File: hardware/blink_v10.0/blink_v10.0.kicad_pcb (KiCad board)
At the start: 2 copper layers, 119 x 92 mm, 129 parts, among them J1 Conn_01x02, J11 KH-BNC50-3511, J12 KH-BNC50-3511, J13 KH-BNC50-3511, J14 Conn_02x16_Odd_Even, J15 Conn_01x01, J16 Conn_01x01, J2 PJ-320D, J3 PJ-320D, J4 KH-BNC50-3511, J5 Conn_01x06_Pin, J6 Conn_01x03, J7 Conn_01x06_Pin, J9 USB_C_Receptacle, Q3 2N7002, Q4 2N7002, Q5 2N7002, SW1 SW_SPDT, SW2 SW_Push_4PDT, SW3 SW_Push_4PDT, SW4 SW_Push_4PDT, U1 AMS1117-3.3, U10 TMP112AIDRLR, U2 AD8397, U3 M24C02-RMN, U4 STM32F405RGTx, U5 SN74LVC1G14DBV, U6 SN74LVC1G14DBV, U7 CH340C, U8 USBLC6-2P6, U9 MCP73832-2-OT, X1 GTXO-14V (2.048MHz), Y1 16MHz

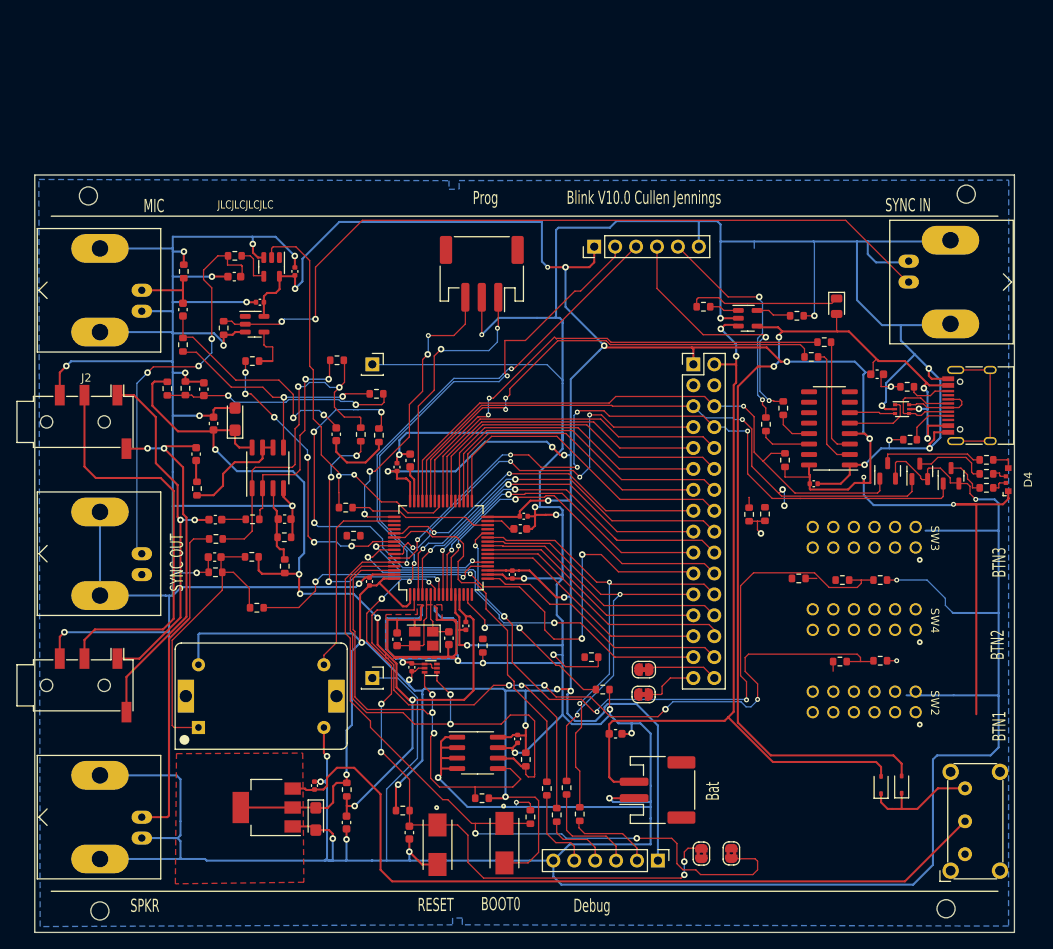
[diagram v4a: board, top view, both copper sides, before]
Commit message: add a sense resistor to blink v10
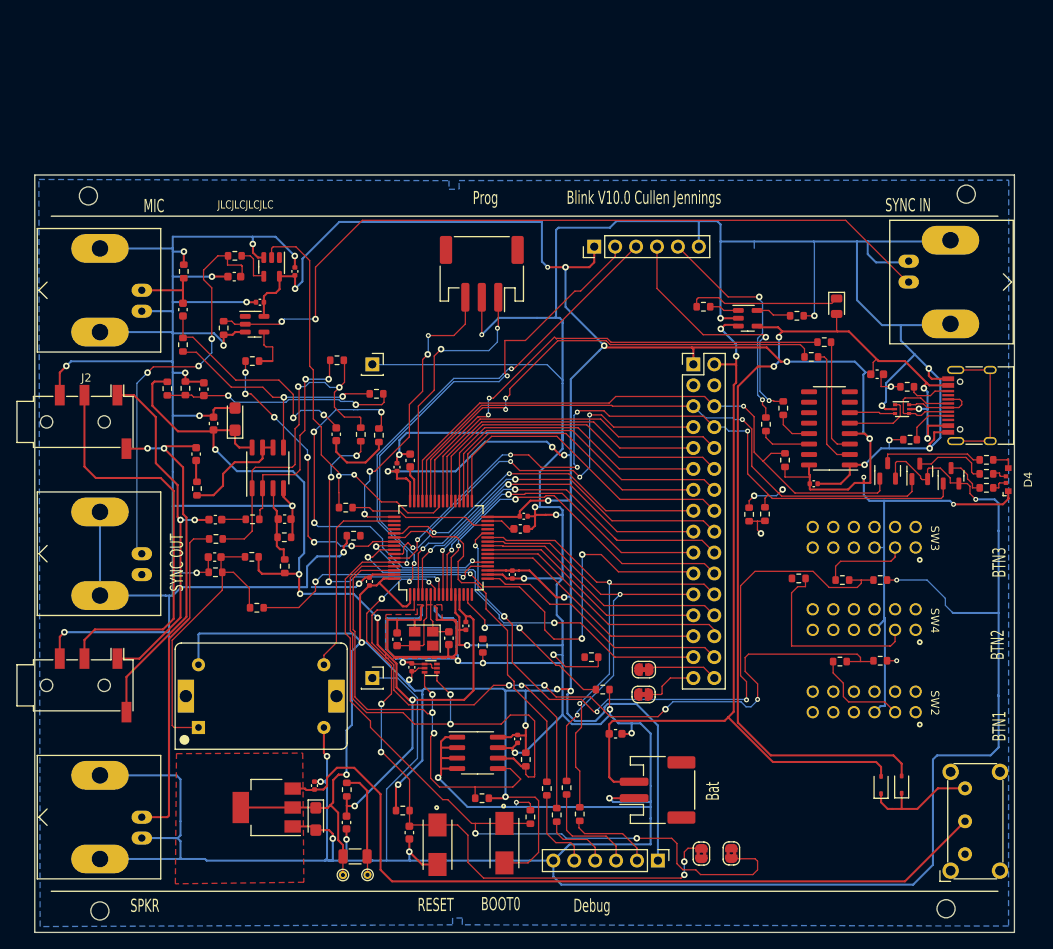
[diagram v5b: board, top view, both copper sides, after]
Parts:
- added R37: 0R1, Resistor_SMD:R_1206_3216Metric, F.Cu at (149.9, 120.8)
- added TP1: ~, TestPoint:TestPoint_THTPad_D1.0mm_Drill0.5mm, F.Cu at (148.4, 123.0)
- added TP2: ~, TestPoint:TestPoint_THTPad_D1.0mm_Drill0.5mm, F.Cu at (151.4, 123.0)
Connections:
- FB1 pad 1: +3.3V -> Net-(FB1-Pad1)
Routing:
- net Net-(R35-Pad1): track 1.38 -> 23.7 mm
- net Net-(FB1-Pad1): track 0.00 -> 13.2 mm
- net Net-(R36-Pad1): track 1.18 -> 11.8 mm
- net GND: track 1085.5 -> 1074.8 mm, vias 46 -> 47
- net Net-(R25-Pad1): track 0.00 -> 10.5 mm
- net +3.3V: track 479.6 -> 490.1 mm
- net /LEDMG: track 79.6 -> 81.8 mm
- net /LEDMB: track 89.5 -> 91.1 mm

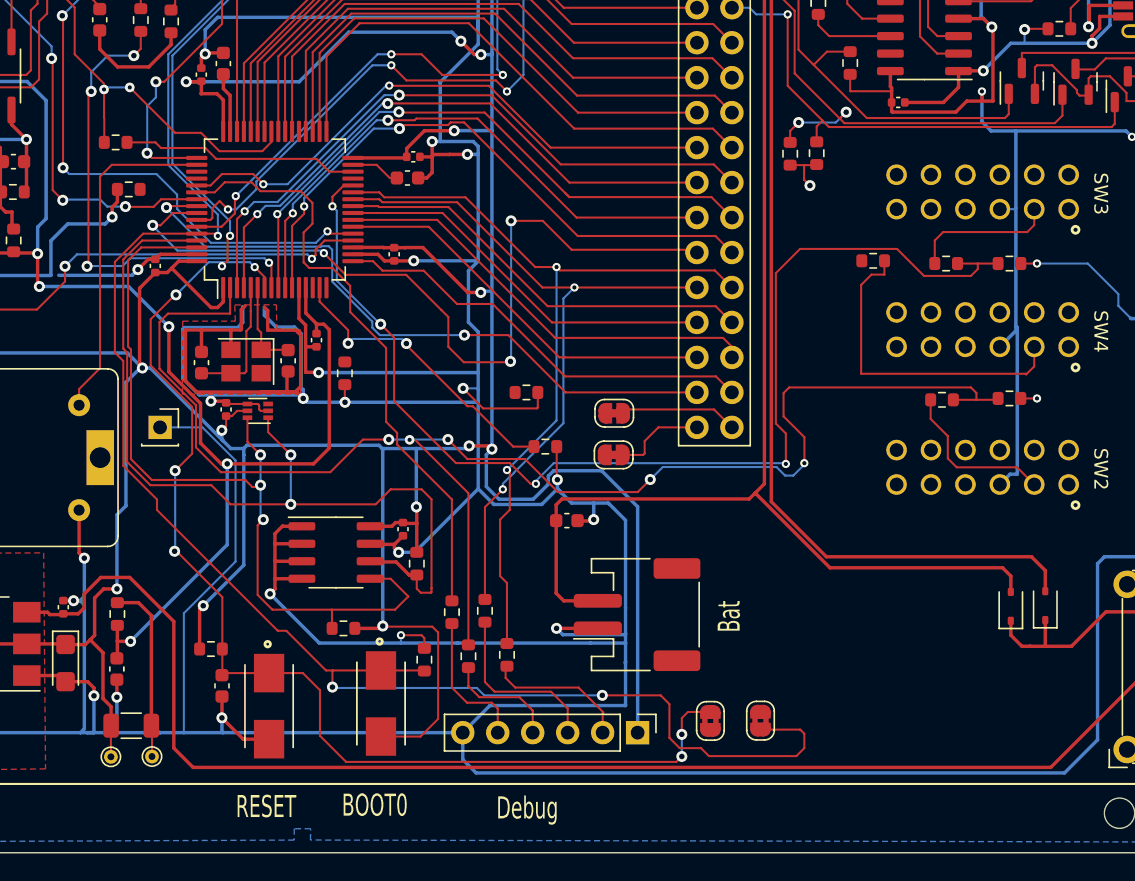
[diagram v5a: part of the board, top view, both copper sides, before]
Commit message: add sense resitors to other ps on bink
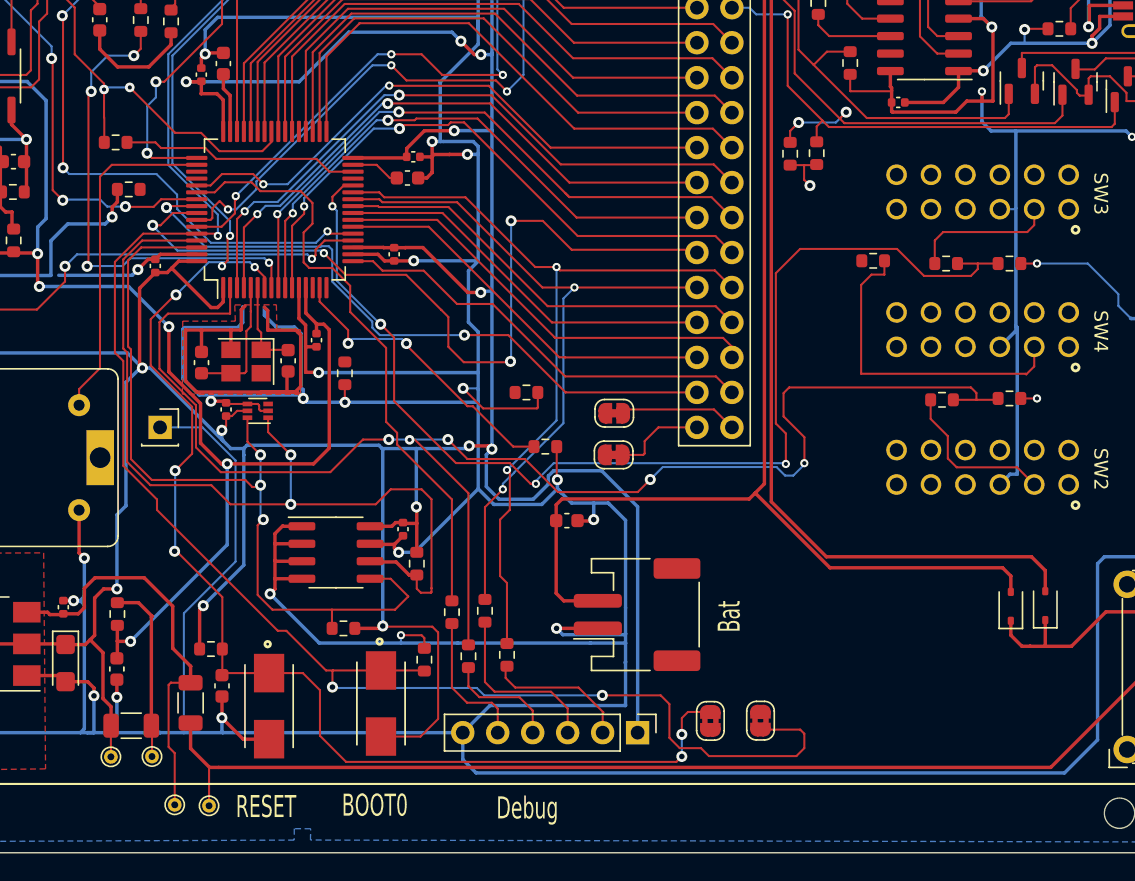
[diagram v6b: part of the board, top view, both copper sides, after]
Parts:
- added R38: 0R1, Resistor_SMD:R_1206_3216Metric, F.Cu at (154.2, 119.1)
- added TP3: ~, TestPoint:TestPoint_THTPad_D1.0mm_Drill0.5mm, F.Cu at (155.6, 126.6)
- added TP4: ~, TestPoint:TestPoint_THTPad_D1.0mm_Drill0.5mm, F.Cu at (153.1, 126.5)
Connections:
- C1 pad 2: Net-(SW1-B) -> Net-(U1-VI)
- SW1 pad 2: Net-(SW1-B) -> +4V
- U1 pad 3: Net-(SW1-B) -> Net-(U1-VI)
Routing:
- net Net-(SW1-B): track 97.5 -> 0.00 mm
- net +4V: track 0.00 -> 78.0 mm
- net Net-(U1-VI): track 0.00 -> 30.0 mm

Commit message: replace power selection diodes with ideal diodes
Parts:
- added U11: MAX40200AUK, Package_TO_SOT_SMD:SOT-23-5, F.Cu at (204.6, 111.2)
- added U12: MAX40200AUK, Package_TO_SOT_SMD:SOT-23-5, F.Cu at (209.7, 111.4)
- moved D2 2.90 mm to (215.7, 109.9)
- moved D3 2.90 mm to (218.2, 109.8)
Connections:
- D2 pad 2: +BATT -> unconnected-(D2-A-Pad2)
- D3 pad 2: VBUS -> unconnected-(D3-A-Pad2)
- SW1 pad 3: Net-(D2-K) -> Net-(SW1-C)
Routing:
- net Net-(SW1-C): track 0.00 -> 23.1 mm
- net GND: track 1074.8 -> 1094.4 mm, vias 47 -> 49
- net Net-(D2-K): track 14.5 -> 5.78 mm
- net +BATT: track 100.0 -> 91.7 mm
- net VBUS: track 118.0 -> 112.5 mm

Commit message: start adding reset circuit to v10 blink
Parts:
- added C31: 100n, Capacitor_SMD:C_0402_1005Metric, F.Cu at (187.1, 29.1)
- added C32: 100n, Capacitor_SMD:C_0402_1005Metric, F.Cu at (187.1, 31.1)
- added C33: 100n, Capacitor_SMD:C_0402_1005Metric, F.Cu at (187.1, 33.1)
- added JP5: SolderJumper_2_Bridged, Jumper:SolderJumper-2_P1.3mm_Bridged2Bar_RoundedPad1.0x1.5mm, F.Cu at (192.0, 19.8)
- added JP6: SolderJumper_2_Bridged, Jumper:SolderJumper-2_P1.3mm_Bridged2Bar_RoundedPad1.0x1.5mm, F.Cu at (198.2, 24.4)
- added R54: 330R, Resistor_SMD:R_0603_1608Metric, F.Cu at (190.6, 29.4)
- added R55: 330R, Resistor_SMD:R_0603_1608Metric, F.Cu at (190.6, 31.9)
- added TP5: ~, TestPoint:TestPoint_THTPad_D1.5mm_Drill0.7mm, F.Cu at (178.8, 22.8)
- added TP6: ~, TestPoint:TestPoint_THTPad_D1.5mm_Drill0.7mm, F.Cu at (178.8, 26.4)
- added TP7: ~, TestPoint:TestPoint_THTPad_D1.5mm_Drill0.7mm, F.Cu at (178.8, 29.9)
- added TP8: ~, TestPoint:TestPoint_THTPad_D1.5mm_Drill0.7mm, F.Cu at (178.8, 33.5)
- added U13: SN74LVC1G14DBV, Package_TO_SOT_SMD:SOT-23-5, F.Cu at (183.1, 23.3)
- added U14: SN74LVC1G14DBV, Package_TO_SOT_SMD:SOT-23-5, F.Cu at (183.1, 27.7)
- added U15: SN74LVC1G14DBV, Package_TO_SOT_SMD:SOT-23-5, F.Cu at (183.1, 32.2)
